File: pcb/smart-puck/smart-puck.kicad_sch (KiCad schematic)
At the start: 13 parts, among them SW1 ILS TA180 40, SW3 ILS TA180 40, U1 Pico

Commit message: Add doorbell socket. oops
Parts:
- added J1: Conn_01x02_Socket, symbol Connector:Conn_01x02_Socket
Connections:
- net at U1.28 (GND): now also J1.2 (Pin_2)
- net at U1.29 (GPIO22): now also J1.1 (Pin_1)
- no-connect marks 36 -> 34
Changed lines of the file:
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@@
-	)
-	(no_connect
-		(at 140.97 115.57)
 	)
 	(no_connect
@@
 	)
 	(no_connect
-		(at 143.51 115.57)
-	)
-	(no_connect
 		(at 151.13 115.57)
 	)
@@
 	(wire
 		(pts
+			(xy 140.97 115.57) (xy 140.97 125.73)
+		)
+		(stroke
+			(width 0)
+			(type default)
+		)
+	)
+	(wire
+		(pts
+			(xy 143.51 115.57) (xy 143.51 123.19)
+		)
+		(stroke
+			(width 0)
+			(type default)
+		)
+	)
+	(wire
+		(pts
 			(xy 168.91 76.2) (xy 194.31 76.2)
 		)
@@
 		(pts
 			(xy 120.65 121.92) (xy 120.65 118.11)
+		)
+		(stroke
+			(width 0)
+			(type default)
+		)
+	)
+	(wire
+		(pts
+			(xy 140.97 125.73) (xy 143.51 125.73)
 		)
 		(stroke
@@
 					(unit 1)
 				)
+			)
+		)
+	)
+	(symbol
+		(lib_id "Connector:Conn_01x02_Socket")
+		(at 148.59 123.19 0)
+		(unit 1)
+		(exclude_from_sim no)
+		(in_bom yes)
+		(on_board yes)
+		(dnp no)
+		(fields_autoplaced yes)
+		(property "Reference" "J1"
+			(at 149.86 123.1899 0)
+			(effects
+				(font
+					(size 1.27 1.27)
+				)
+				(justify left)
+			)
+		)
+		(property "Value" "Conn_01x02_Socket"
+			(at 149.86 125.7299 0)
+			(effects
+				(font
+					(size 1.27 1.27)
+				)
+				(justify left)
+			)
+		)
+		(property "Footprint" ""
+			(at 148.59 123.19 0)
+			(effects
+				(font
+					(size 1.27 1.27)
+				)
+				(hide yes)
+			)
+		)
+		(property "Datasheet" "~"
+			(at 148.59 123.19 0)
+			(effects
+				(font
+					(size 1.27 1.27)
+				)
+				(hide yes)
+			)
+		)
+		(property "Description" "Generic connector, single row, 01x02, script generated"
+			(at 148.59 123.19 0)
+			(effects
+				(font
+					(size 1.27 1.27)
+				)
+				(hide yes)
+			)
+		)
+		(pin "2"
+		)
+		(pin "1"
+		)
+		(instances
+			(project ""
+				(path "/7e615054-cce3-47a9-a337-7924894bf240"
+					(reference "J1")
+					(unit 1)
+				)

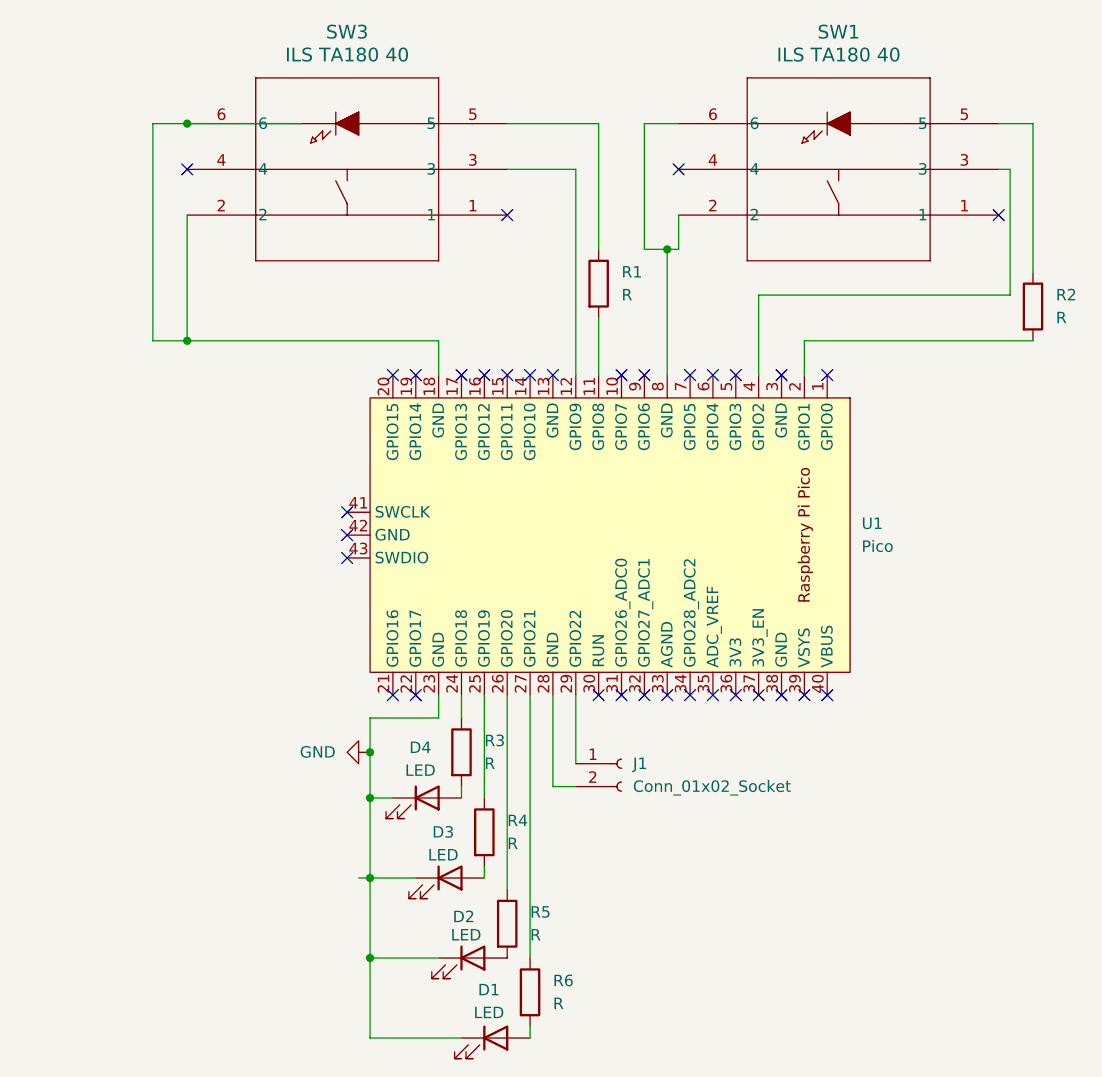
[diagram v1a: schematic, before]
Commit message: update PCB. Align components. Add some mounting holes. Add a big hole in case we need to mount the doorbell stuff underneath
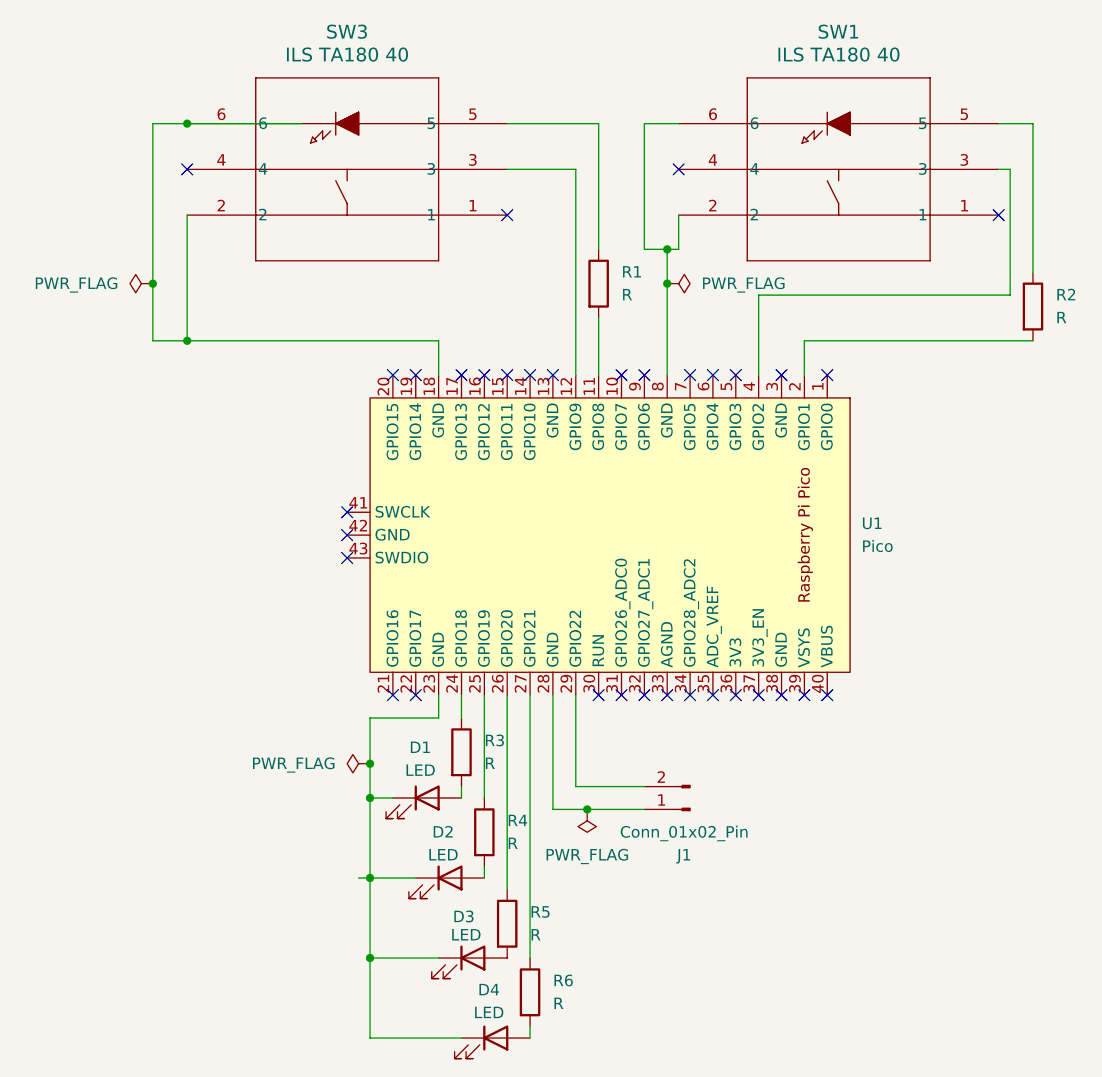
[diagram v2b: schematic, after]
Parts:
- removed J1: Conn_01x02_Socket, symbol Connector:Conn_01x02_Socket
- added J1: Conn_01x02_Pin, Connector_PinHeader_2.54mm:PinHeader_1x02_P2.54mm_Vertical, symbol Connector:Conn_01x02_Pin
- renumbered D4 to D1, D3 to D2, D2 to D3, D1 to D4
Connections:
- net at U1.29 (GPIO22): now also J1.2 (Pin_2)
- net at U1.28 (GND): now also J1.1 (Pin_1)
- net GND: no longer names the net of D1.1 (K), D2.1 (K), D3.1 (K), D4.1 (K), U1.23 (GND)
